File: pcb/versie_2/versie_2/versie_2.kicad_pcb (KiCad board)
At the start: 2 copper layers, 32 x 61 mm, 3 parts, among them J2 Conn_01x04_Pin, J3 B4B-PH-SM4-TB__LF__SN_, U1 DFR0478

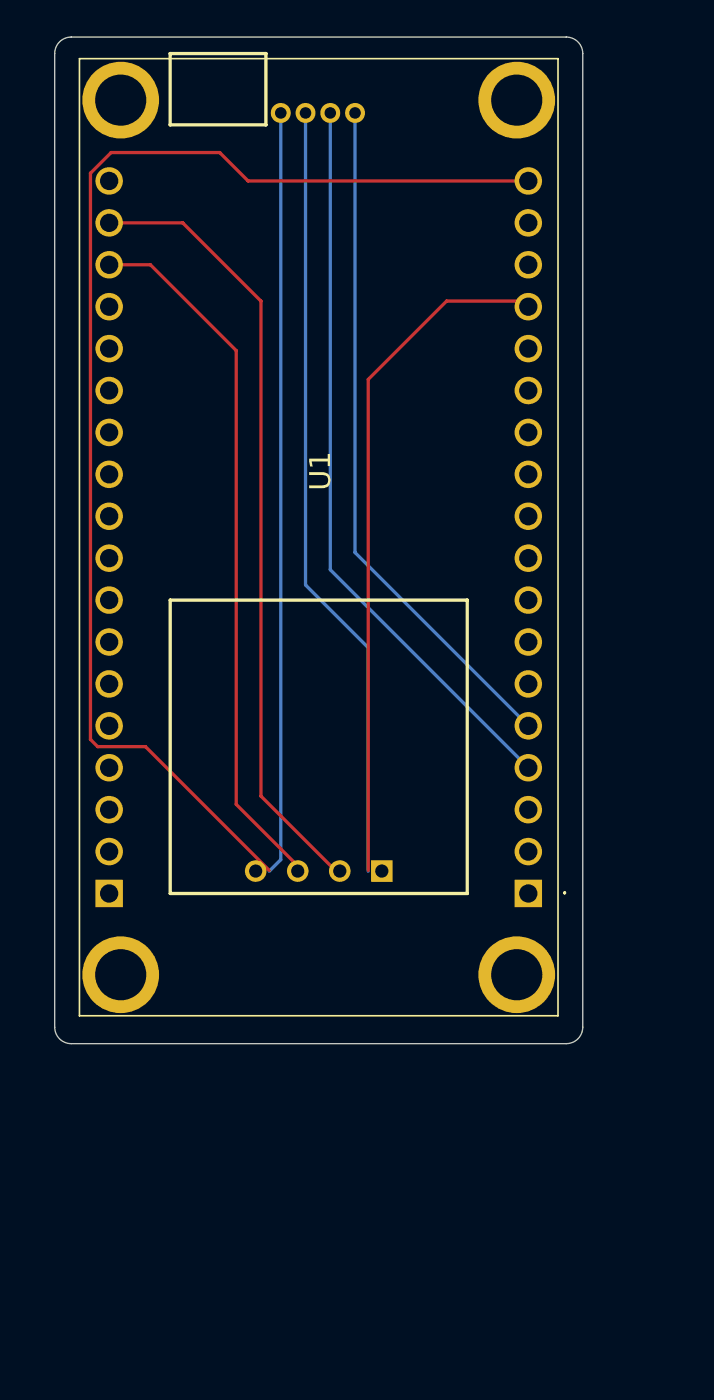
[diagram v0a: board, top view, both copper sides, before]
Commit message: pcb mod
aanpassing aan de pcb zodat de gps kan geplaatst worden.
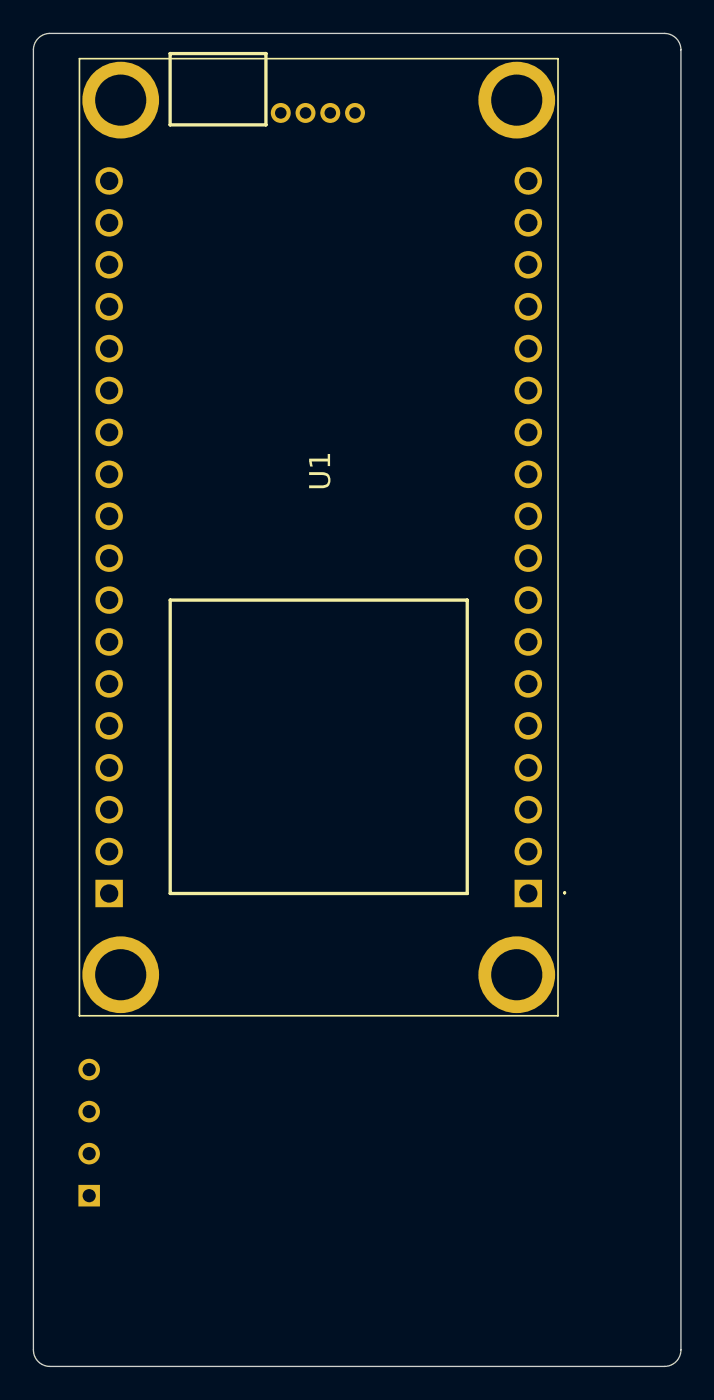
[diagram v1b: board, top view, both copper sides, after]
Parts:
- moved J2 33.0 mm to (205.1, 116.9), turned to -90 degrees
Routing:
- net vcc: track 122.5 -> 0.00 mm
- net GND: track 89.2 -> 0.48 mm
- net TX: track 47.5 -> 0.00 mm
- net RX_1: track 44.8 -> 0.00 mm
- net RX: track 43.0 -> 0.00 mm
- net TX_1: track 41.6 -> 0.20 mm
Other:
- board size 32 x 61 mm -> 39.2 x 80.8 mm

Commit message: aanpassing
voorstel
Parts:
- added ?: , , F.Cu at (190.5, 118.7)
- added ?: , , F.Cu at (190.5, 69.6)
- added ?: , , F.Cu at (132.4, 118.5)
- added ?: , , F.Cu at (132.4, 69.4)
- moved U1 91.8 mm to (111.5, 92.5)
- moved J3 91.8 mm to (107.7, 71.9)
- moved J2 59.6 mm to (149.1, 96.5)
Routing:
- net GND: track 0.48 -> 47.2 mm
- net TX: track 0.00 -> 45.3 mm
- net RX_1: track 0.00 -> 44.7 mm
- net TX_1: track 0.20 -> 41.7 mm
- net RX: track 0.00 -> 39.7 mm
- net vcc: track 0.00 -> 39.1 mm
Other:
- board size 39.2 x 80.8 mm -> 100 x 63.5 mm

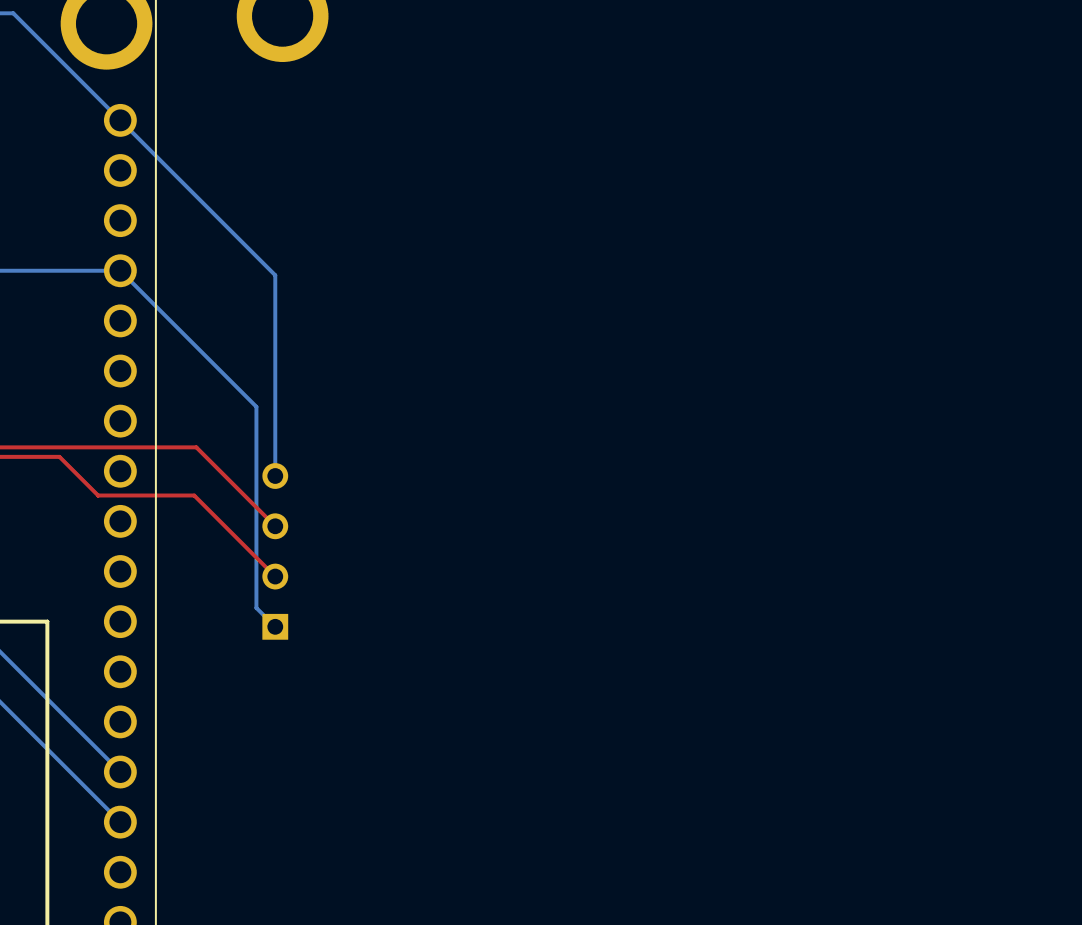
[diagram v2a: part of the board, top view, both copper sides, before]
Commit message: pcb
omdraaien tb600
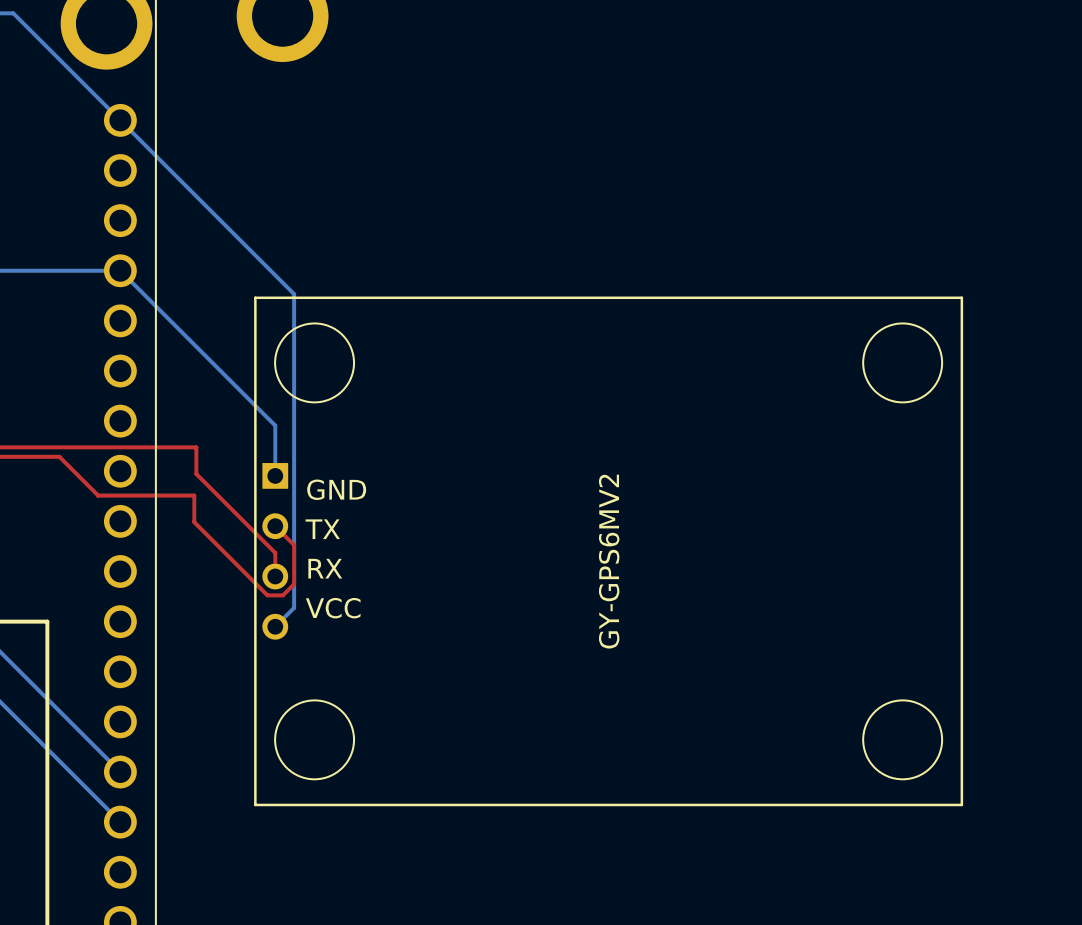
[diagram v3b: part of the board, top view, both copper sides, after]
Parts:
- J2: moved to F.Cu
- turned J2 to 90 degrees
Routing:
- net vcc: track 39.1 -> 47.5 mm
- net GND: track 47.2 -> 39.6 mm
- net TX: track 45.3 -> 51.0 mm
- net RX: track 39.7 -> 42.2 mm

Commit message: pcb_update
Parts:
- removed ? (x4): , 
- added H1: MountingHole_Pad, MountingHole:MountingHole_3.2mm_M3_ISO14580_Pad_TopBottom, F.Cu at (189.8, 71.8)
- added H2: MountingHole_Pad, MountingHole:MountingHole_3.2mm_M3_ISO14580_Pad_TopBottom, F.Cu at (131.7, 71.6)
- added H3: MountingHole_Pad, MountingHole:MountingHole_3.2mm_M3_ISO14580_Pad_TopBottom, F.Cu at (131.7, 120.7)
- added H4: MountingHole_Pad, MountingHole:MountingHole_3.2mm_M3_ISO14580_Pad_TopBottom, F.Cu at (189.8, 120.9)
- added H5: MountingHole_Pad, MountingHole:MountingHole_3.2mm_M3_ISO14580_Pad_TopBottom, F.Cu at (189.7, 84.5)
- added H6: MountingHole_Pad, MountingHole:MountingHole_3.2mm_M3_ISO14580_Pad_TopBottom, F.Cu at (159.8, 84.5)
- added H7: MountingHole_Pad, MountingHole:MountingHole_3.2mm_M3_ISO14580_Pad_TopBottom, F.Cu at (159.8, 103.7)
- added H8: MountingHole_Pad, MountingHole:MountingHole_3.2mm_M3_ISO14580_Pad_TopBottom, F.Cu at (189.7, 103.7)
- J3: moved to F.Cu
- moved J2 26.0 mm to (174.9, 94.1)
- moved J3 7.49 mm to (115.2, 71.9), turned to 180 degrees
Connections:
- U1 pad MH1: unconnected-(U1-PadMH1) -> GND
- U1 pad MH2: unconnected-(U1-PadMH2) -> GND
- U1 pad MH3: unconnected-(U1-PadMH3) -> GND
- U1 pad MH4: unconnected-(U1-PadMH4) -> GND
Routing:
- net RX: track 42.2 -> 65.5 mm
- net GND: track 39.6 -> 17.4 mm
- net TX: track 51.0 -> 65.5 mm
- net TX_1: track 41.7 -> 52.9 mm
- net vcc: track 47.5 -> 55.7 mm
- net RX_1: track 44.7 -> 45.3 mm
- added copper zone on F.Cu, net GND
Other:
- board size 100 x 63.5 mm -> 101 x 63.5 mm
- board text added: "Solar Power Manager"
